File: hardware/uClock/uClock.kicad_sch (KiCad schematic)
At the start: 27 parts, among them J1 USB_B_Micro, J3 SSD1306, Q1 BSS138, Q2 BSS138, Q4 AO3401A, SW1 BUTTON, U1 ESP8285, U2 DS3231MZ, U3 TP4056, U4 CH340C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

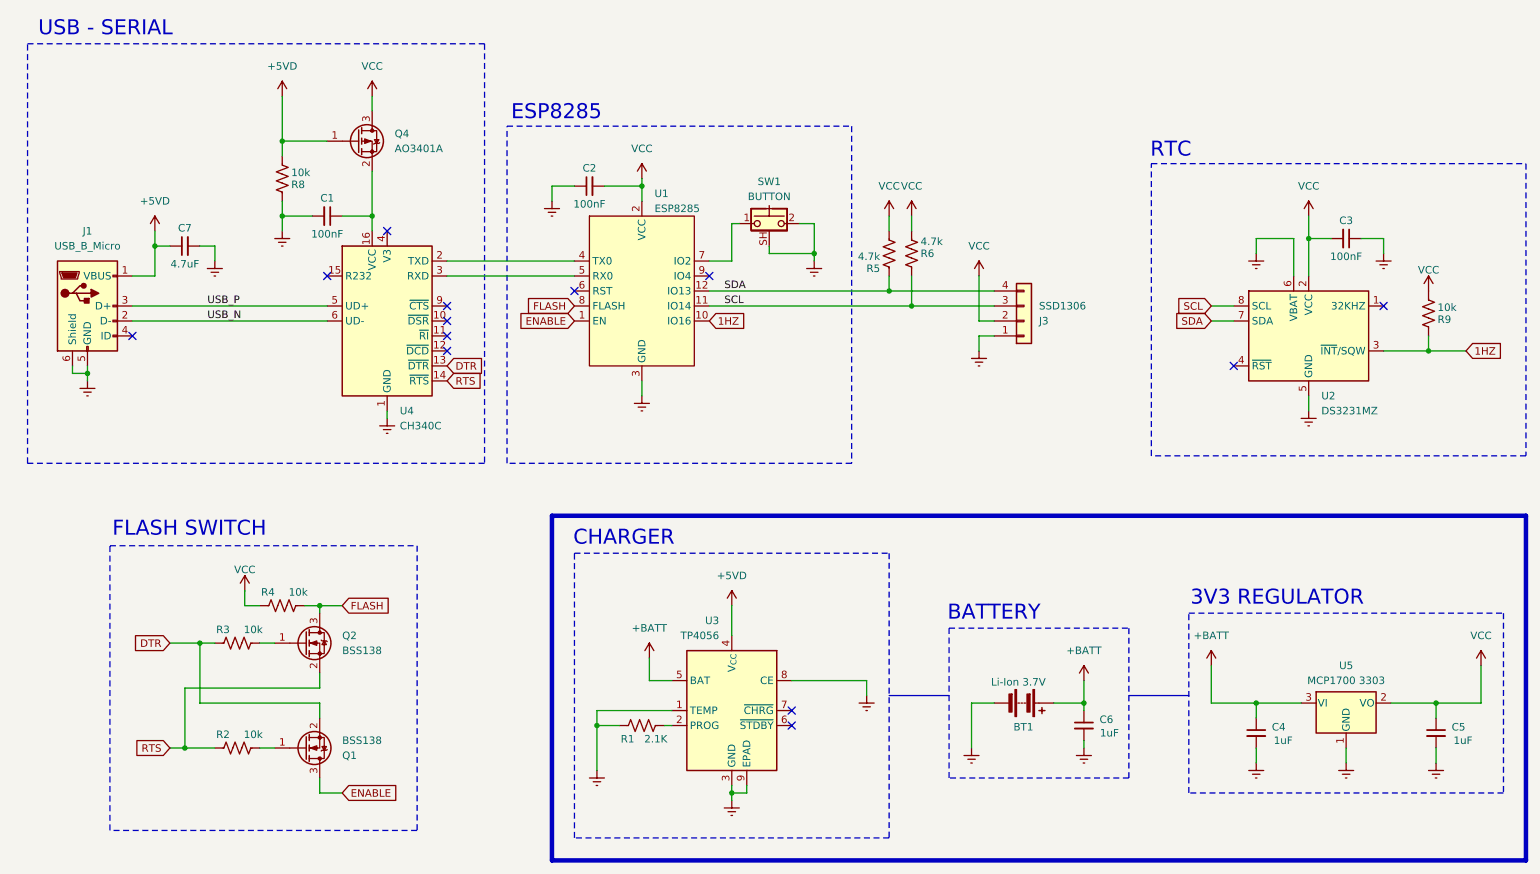
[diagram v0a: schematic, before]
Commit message: PCB Update - rev2
- CH340 power corrected
- Optimized RTC conspumtion
- Pullup added to SW1
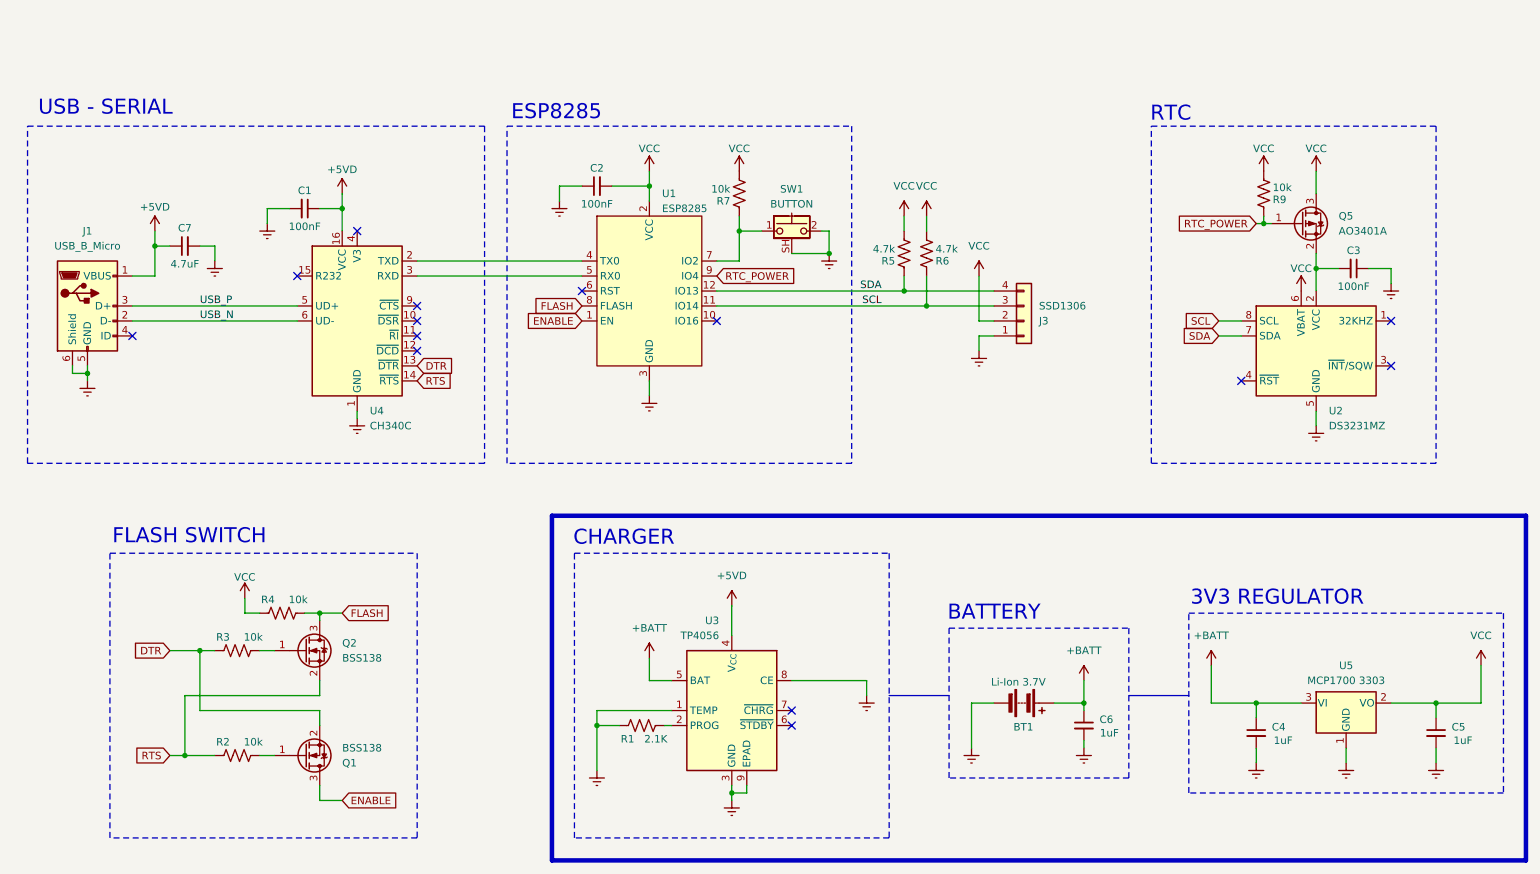
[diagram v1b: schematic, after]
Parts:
- removed Q4: AO3401A, Package_TO_SOT_SMD:SOT-23, symbol Transistor_FET:AO3401A
- removed R8: 10k, Resistor_SMD:R_0603_1608Metric_Pad0.98x0.95mm_HandSolder, symbol Device:R_US
- added Q5: AO3401A, Package_TO_SOT_SMD:SOT-23, symbol Transistor_FET:AO3401A
- added R7: 10k, Resistor_SMD:R_0603_1608Metric_Pad0.98x0.95mm_HandSolder, symbol Device:R_US
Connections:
- net +5VD: now also C1.1, U4.16 (VCC)
- net Earth: no longer U2.6 (VBAT)
- net VCC: now also U2.6 (VBAT), Q5.3 (D), R7.2; no longer C3.2, U2.2 (VCC)
- net at SW1.1, U1.7 (IO2): now also R7.1
- net RTC_POWER: now reaches U1.9 (IO4)
- net RTC_POWER: now also R9.1, Q5.1 (G)
- removed net 1HZ: R9.1, U1.10 (IO16), U2.3 (~{INT}/SQW)
- new net: C3.2, Q5.2 (S), U2.2 (VCC)
- no-connect marks 13 -> 14
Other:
- moved on the sheet: C1, C2, C3, Q1, Q2, R2, R3, R4, R5, R6, SW1, U1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
